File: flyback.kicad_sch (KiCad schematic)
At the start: 41 parts, among them Q1 BSC109N10NS3G, Q2 STN3N40K3, Q3 IGB50N65S, Q4 IGB50N65S, U1 LT3750EMSTR, U3 NCS325, U301 IX4427MTR, U5 IX4427MTR

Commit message: Use parts similar to the main pcb where possible.
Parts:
- R16: MPN RMCF0603FT1K00 -> RC0603FR-101KL
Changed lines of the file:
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@@
       (effects (font (size 1.27 1.27)) hide)
     )
-    (property "MPN" "RMCF0603FT1K00" (at 154.94 100.33 0)
+    (property "MPN" "RC0603FR-101KL" (at 154.94 100.33 0)
       (effects (font (size 1.27 1.27)) hide)
     )

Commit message: Add missing MPNs.
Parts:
- RV301: MPN (none) -> TC33X-2-503E
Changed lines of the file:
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@@
+      (effects (font (size 1.27 1.27)) hide)
+    )
+    (property "MPN" "TC33X-2-503E" (at 111.76 78.74 0)
       (effects (font (size 1.27 1.27)) hide)
     )

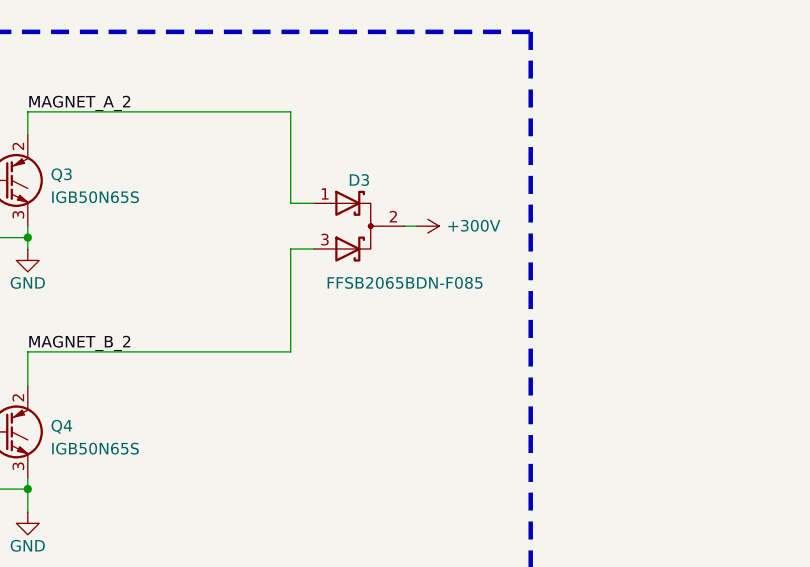
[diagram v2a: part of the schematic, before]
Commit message: Change the parts that were not in stock.
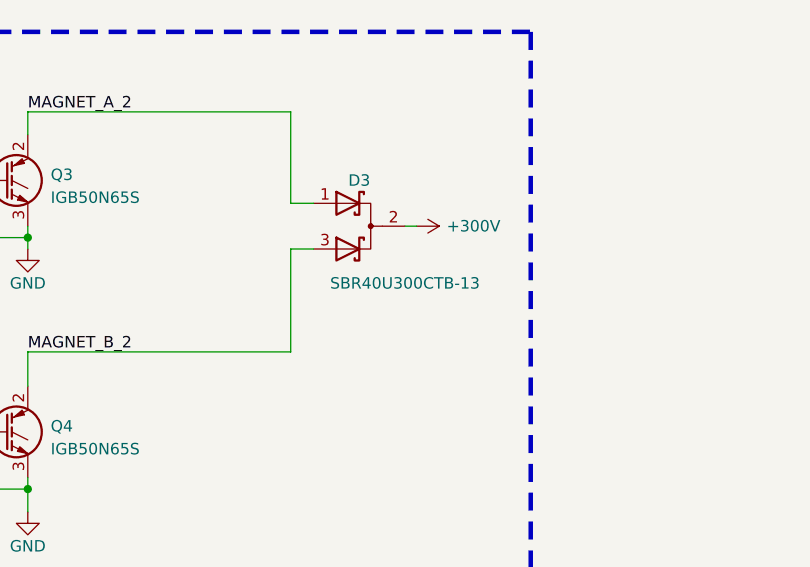
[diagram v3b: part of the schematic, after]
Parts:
- C1, C13, C301: JLCPCB Comment 10uF 50V X5R -> (none); JLCPCB Footprint 0805 -> (none)
- C10, C21, C302: JLCPCB Comment 100nF 50V X7R -> (none); JLCPCB Footprint 0402 -> (none)
- C2: JLCPCB Comment 10nF 35V X5R -> (none); JLCPCB Footprint 0603 -> (none)
- C3, C9: JLCPCB Comment 100pF 50V -> (none); JLCPCB Footprint 0402 -> (none)
- C4, C5, C6: JLCPCB Comment 22uF 25V X7R -> (none); JLCPCB Footprint 1210 -> (none)
- C7: JLCPCB Comment 180uF 35V -> (none); JLCPCB Footprint E12 -> (none)
- C8: JLCPCB Comment 100nF 630V X7R -> (none); JLCPCB Footprint 1812 -> (none)
- D1: JLCPCB Comment MURS160A -> (none); JLCPCB Footprint SMA -> (none)
- D2, D5: JLCPCB Comment SMBJ13CA-13-F -> (none); JLCPCB Footprint SMB -> (none)
- D3: value FFSB2065BDN-F085 -> SBR40U300CTB-13; JLCPCB Comment FFSB2065BDN-F085 -> (none); MPN FFSB2065BDN-F085 -> SBR40U300CTB-13
- Q1: JLCPCB Comment BSC109N10NS3 G -> (none)
- Q2: JLCPCB Comment STN3N40K3 -> (none)
- Q3, Q4: JLCPCB Comment IGB50N65S5ATMA1 -> (none)
- R1: JLCPCB Comment 43KΩ %5 -> (none); JLCPCB Footprint 0402 -> (none)
- R10, R11, R9: JLCPCB Comment 2.4KΩ 1% 3W -> (none); JLCPCB Footprint 2512 -> (none)
- R14: JLCPCB Comment 10MΩ 1% -> (none); JLCPCB Footprint 0603 -> (none)
- R15: JLCPCB Comment 100KΩ 1% -> (none); JLCPCB Footprint 0402 -> (none)
- R16: JLCPCB Comment 1KΩ 1% -> (none); JLCPCB Footprint 0603 -> (none)
- R17, R4, R8: JLCPCB Comment 10Ω 5% -> (none); JLCPCB Footprint 0402 -> (none)
- R3: JLCPCB Comment 40.2KΩ 1% -> (none); JLCPCB Footprint 0402 -> (none)
- R6: JLCPCB Comment 2.49KΩ 1% -> (none); JLCPCB Footprint 0402 -> (none)
- R7: JLCPCB Comment 10mΩ 1% 3/4W -> (none); JLCPCB Footprint 0805 -> (none)
- U1: JLCPCB Comment LT3750EMS -> (none)
- U3: JLCPCB Comment NCS325SN2T1G -> (none)
- U301, U5: JLCPCB Comment IX4427MTR -> (none)
